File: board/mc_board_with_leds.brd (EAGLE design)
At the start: 73.8 x 40.1 mm, 36 parts, among them IC1 TPS61070DDC, IC2 MEGA8-P, Q2 16MHz

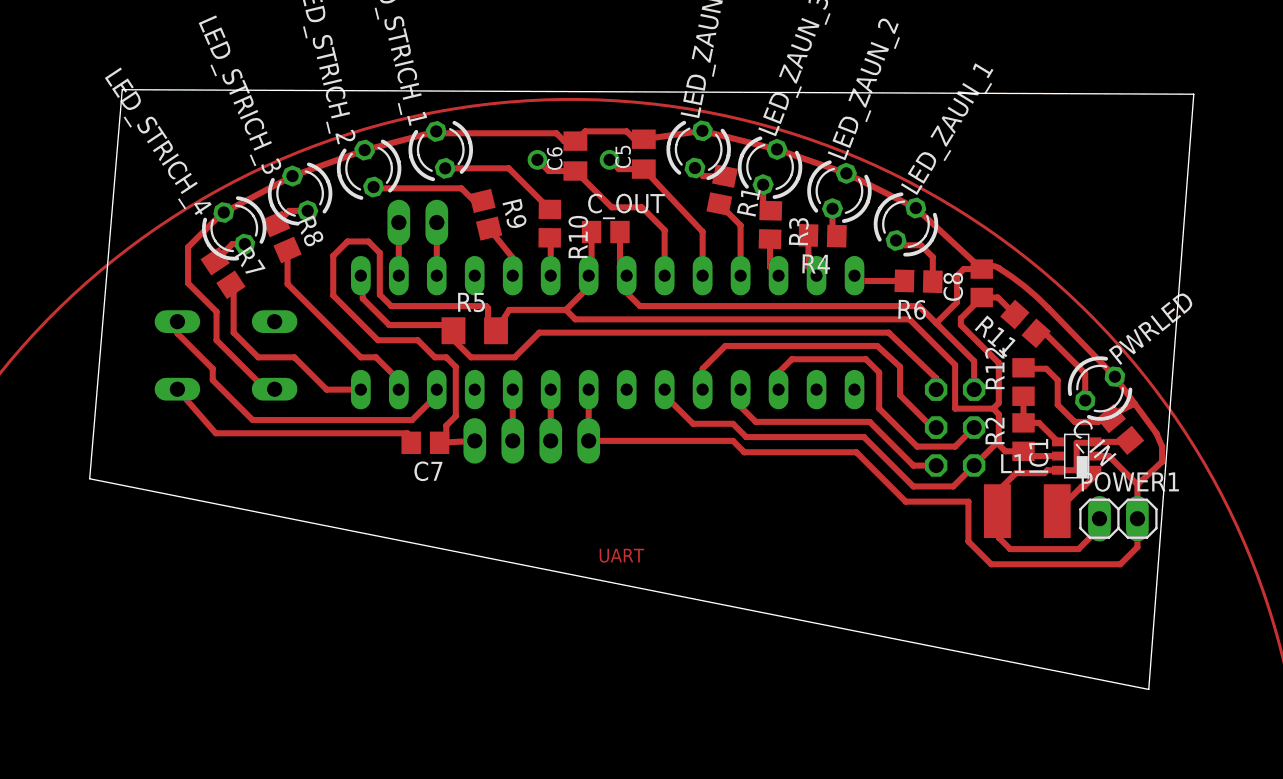
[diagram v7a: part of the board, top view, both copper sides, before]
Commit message: added names to board
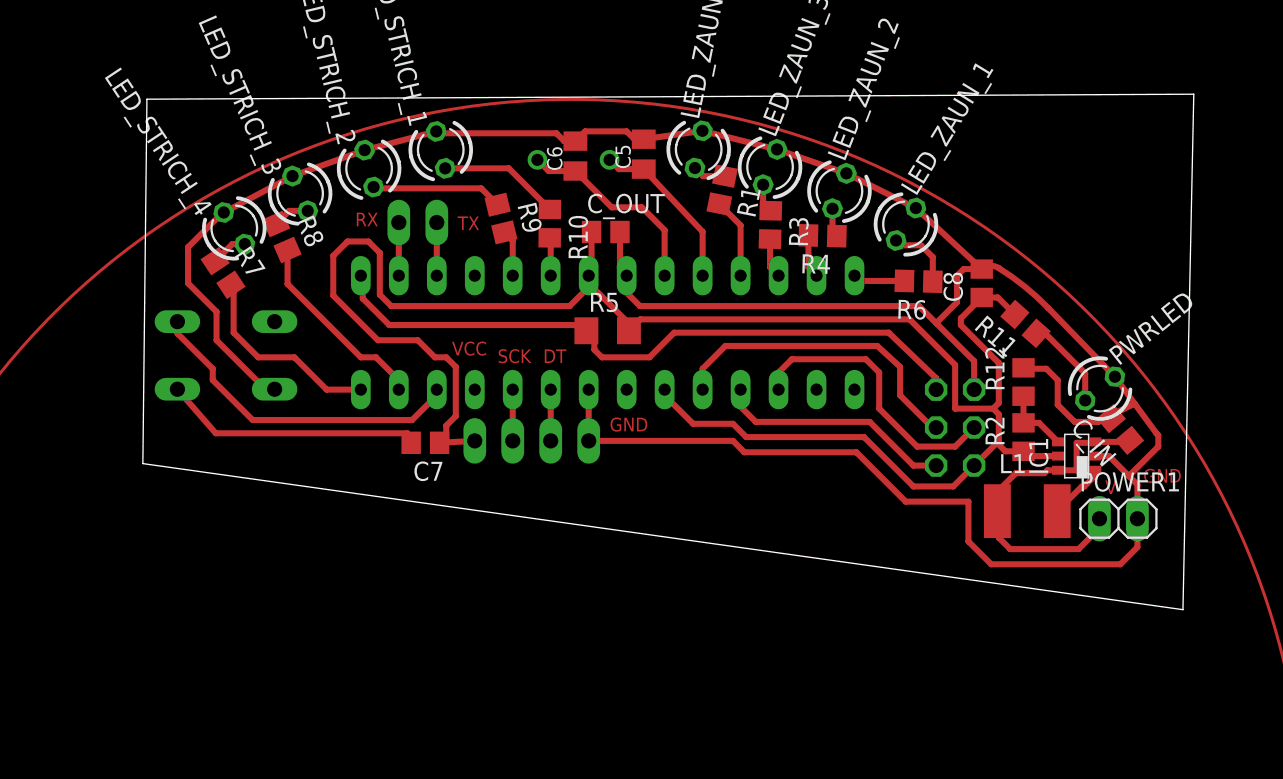
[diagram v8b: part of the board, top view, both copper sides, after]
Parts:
- moved R5 8.89 mm to (51.4, 33.5)
- moved R9 1.05 mm to (44.3, 41.0)
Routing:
- net +5V: track 126.5 -> 124.4 mm
- net N$11: track 7.67 -> 8.79 mm
- net PD3/LED_STRICH_2: track 3.71 -> 3.13 mm
- net GND: track 192.8 -> 192.3 mm
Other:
- board size 73.8 x 40.1 mm -> 70.3 x 34.5 mm
- board text added: "DT"
- board text added: "GND"
- board text added: "RX"
- board text added: "SCK"
- board text added: "TX"
- board text added: "V"
- board text added: "VCC"
- board text removed: "UART"
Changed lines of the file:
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@@
 <board>
 <plain>
-<text x="50.8" y="18.034" size="0.9144" layer="1" font="vector" ratio="28">UART</text>
-<wire x1="16.789471875" y1="23.62764375" x2="18.966596875" y2="49.651115625" width="0" layer="20"/>
-<wire x1="18.966596875" y1="49.651115625" x2="90.63675" y2="49.349575" width="0" layer="20"/>
-<wire x1="90.63675" y1="49.349575" x2="87.626409375" y2="9.53845" width="0" layer="20"/>
-<wire x1="87.626409375" y1="9.53845" x2="16.789471875" y2="23.62764375" width="0" layer="20"/>
+<wire x1="20.345471875" y1="24.64364375" x2="20.617596875" y2="49.016115625" width="0" layer="20"/>
+<wire x1="20.617596875" y1="49.016115625" x2="90.63675" y2="49.349575" width="0" layer="20"/>
+<wire x1="90.63675" y1="49.349575" x2="89.912409375" y2="14.87245" width="0" layer="20"/>
+<wire x1="89.912409375" y1="14.87245" x2="20.345471875" y2="24.64364375" width="0" layer="20"/>
 <circle x="49" y="0" radius="49" width="0.2" layer="1"/>
+<text x="34.544" y="40.513" size="0.9144" layer="1" font="vector" ratio="28">RX</text>
+<text x="41.402" y="40.259" size="0.9144" layer="1" font="vector" ratio="28">TX</text>
+<text x="51.562" y="26.797" size="0.9144" layer="1" font="vector" ratio="28">GND</text>
+<text x="87.249" y="23.368" size="0.9144" layer="1" font="vector" ratio="28">GND</text>
+<text x="84.709" y="22.606" size="0.9144" layer="1" font="vector" ratio="28">V</text>
+<text x="47.117" y="31.369" size="0.9144" layer="1" font="vector" ratio="28">DT</text>
+<text x="44.069" y="31.369" size="0.9144" layer="1" font="vector" ratio="28">SCK</text>
+<text x="41.021" y="31.877" size="0.9144" layer="1" font="vector" ratio="28">VCC</text>
 </plain>
 <attributes>
@@
 <element name="R7" library="resistor" package="R0805" value="470" x="25.7096625" y="37.39071875" rot="R303.6"/>
 <element name="R8" library="resistor" package="R0805" value="470" x="29.6424875" y="39.798434375" rot="R293.6"/>
-<element name="R9" library="resistor" package="R0805" value="470" x="43.281534375" y="41.287296875" rot="R283.6"/>
+<element name="R9" library="resistor" package="R0805" value="470" x="44.297534375" y="41.033296875" rot="R283.6"/>
 <element name="R10" library="resistor" package="R0805" value="470" x="47.565540625" y="40.692409375" rot="R269.6"/>
 <element name="R11" library="resistor" package="R0805" value="470" x="79.383846875" y="33.986165625" rot="R138.6"/>
@@
 <attribute name="OC_FARNELL" value="176432" x="36.703" y="26.162" size="1.778" layer="28" rot="MR0" display="off"/>
 </element>
-<element name="R5" library="rcl-2" package="R1206" value="10k" x="42.545" y="33.528"/>
+<element name="R5" library="rcl-2" package="R1206" value="10k" x="51.435" y="33.528"/>
 <element name="ISP1" library="con-panduit" package="057-006-1" value="ISP-Connector" x="74.676" y="27.051" rot="MR90">
 <attribute name="MPN" value="" x="25.527" y="16.383" size="1.778" layer="28" rot="MR90" display="off"/>
@@
 <wire x1="25.691109375" y1="41.439109375" x2="25.757203125" y2="41.439109375" width="0.4064" layer="1"/>
 <wire x1="84.054" y1="25.146" x2="84.963" y2="25.146" width="0.4064" layer="1"/>
-<wire x1="84.963" y1="25.146" x2="86.868" y2="23.241" width="0.4064" layer="1"/>
+<wire x1="84.963" y1="25.146" x2="86.2965" y2="23.8125" width="0.4064" layer="1"/>
+<wire x1="86.2965" y1="23.8125" x2="86.868" y2="23.241" width="0.4064" layer="1"/>
 <wire x1="86.868" y1="23.241" x2="86.868" y2="20.955" width="0.4064" layer="1"/>
 <wire x1="85.360259375" y1="30.4531125" x2="86.6831" y2="28.651484375" width="0.4064" layer="1"/>
 <wire x1="86.6831" y1="28.651484375" x2="88.138" y2="26.67" width="0.4064" layer="1"/>
-<wire x1="88.138" y1="26.67" x2="88.519" y2="25.781" width="0.4064" layer="1"/>
-<wire x1="88.519" y1="25.781" x2="88.519" y2="24.765" width="0.4064" layer="1"/>
-<wire x1="88.519" y1="24.765" x2="86.868" y2="23.241" width="0.4064" layer="1"/>
 <wire x1="84.201" y1="27.432" x2="85.11435" y2="27.651740625" width="0.4064" layer="1"/>
 <wire x1="84.201" y1="27.432" x2="86.6831" y2="28.651484375" width="0.4064" layer="1"/>
+<wire x1="88.138" y1="26.67" x2="88.265" y2="26.543" width="0.4064" layer="1"/>
+<wire x1="88.265" y1="26.543" x2="88.265" y2="25.781" width="0.4064" layer="1"/>
+<wire x1="88.265" y1="25.781" x2="86.2965" y2="23.8125" width="0.4064" layer="1"/>
 </signal>
 <signal name="+5V">
@@
 <contactref element="HX1" pad="4"/>
 <wire x1="50.165" y1="37.211" x2="50.165" y2="36.449" width="0.4064" layer="1"/>
-<wire x1="50.165" y1="36.449" x2="48.641" y2="34.925" width="0.4064" layer="1"/>
-<wire x1="48.641" y1="34.925" x2="44.856" y2="34.925" width="0.4064" layer="1"/>
-<wire x1="44.856" y1="34.925" x2="43.967" y2="33.528" width="0.4064" layer="1"/>
-<wire x1="48.641" y1="34.925" x2="49.276" y2="34.29" width="0.4064" layer="1"/>
-<wire x1="49.276" y1="34.29" x2="71.628" y2="34.29" width="0.4064" layer="1"/>
 <wire x1="71.628" y1="34.29" x2="74.676" y2="31.242" width="0.4064" layer="1"/>
 <wire x1="74.676" y1="31.242" x2="74.676" y2="28.321" width="0.4064" layer="1"/>
@@
 <wire x1="77.597" y1="26.162" x2="77.47" y2="26.035" width="0.4064" layer="1"/>
 <wire x1="77.47" y1="26.035" x2="75.946" y2="24.511" width="0.4064" layer="1"/>
-<wire x1="43.967" y1="33.528" x2="43.434" y2="34.061" width="0.4064" layer="1"/>
-<wire x1="43.434" y1="34.061" x2="43.434" y2="35.052" width="0.4064" layer="1"/>
-<wire x1="43.434" y1="35.052" x2="43.307" y2="35.179" width="0.4064" layer="1"/>
-<wire x1="43.307" y1="35.179" x2="36.957" y2="35.179" width="0.4064" layer="1"/>
 <wire x1="36.957" y1="35.179" x2="36.195" y2="35.941" width="0.4064" layer="1"/>
 <wire x1="36.195" y1="35.941" x2="36.195" y2="38.735" width="0.4064" layer="1"/>
@@
 <wire x1="79.248" y1="25.466" x2="78.039" y2="25.466" width="0.4064" layer="1"/>
 <wire x1="78.039" y1="25.466" x2="77.47" y2="26.035" width="0.4064" layer="1"/>
+<wire x1="71.628" y1="34.29" x2="53.619" y2="34.29" width="0.4064" layer="1"/>
+<wire x1="50.165" y1="36.449" x2="48.895" y2="35.179" width="0.4064" layer="1"/>
+<wire x1="48.895" y1="35.179" x2="36.957" y2="35.179" width="0.4064" layer="1"/>
+<wire x1="53.619" y1="34.29" x2="52.857" y2="33.528" width="0.4064" layer="1"/>
+<wire x1="50.165" y1="36.449" x2="50.419" y2="36.449" width="0.4064" layer="1"/>
+<wire x1="50.419" y1="36.449" x2="52.578" y2="34.29" width="0.4064" layer="1"/>
+<wire x1="52.578" y1="34.29" x2="52.578" y2="33.807" width="0.4064" layer="1"/>
+<wire x1="52.578" y1="33.807" x2="52.857" y2="33.528" width="0.4064" layer="1"/>
 </signal>
 <signal name="PB4/MISO">
@@
 <contactref element="IC2" pad="5"/>
 <contactref element="R9" pad="2"/>
-<wire x1="45.085" y1="37.211" x2="45.085" y2="38.40285" width="0.4064" layer="1"/>
-<wire x1="45.085" y1="38.40285" x2="43.50491875" y2="40.36393125" width="0.4064" layer="1"/>
+<wire x1="45.085" y1="37.211" x2="45.085" y2="37.719" width="0.4064" layer="1"/>
+<wire x1="45.085" y1="37.719" x2="45.085" y2="38.40285" width="0.4064" layer="1"/>
+<wire x1="44.52091875" y1="40.10993125" x2="45.085" y2="39.54585" width="0.4064" layer="1"/>
+<wire x1="45.085" y1="39.54585" x2="45.085" y2="38.40285" width="0.4064" layer="1"/>
 </signal>
 <signal name="PD4/LED_STRICH_1">
@@
 <wire x1="73.406" y1="29.591" x2="73.406" y2="30.353" width="0.4064" layer="1"/>
 <wire x1="73.406" y1="30.353" x2="70.231" y2="33.401" width="0.4064" layer="1"/>
-<wire x1="70.231" y1="33.401" x2="46.863" y2="33.401" width="0.4064" layer="1"/>
-<wire x1="46.863" y1="33.401" x2="45.212" y2="31.75" width="0.4064" layer="1"/>
-<wire x1="40.996" y1="33.045" x2="41.123" y2="33.528" width="0.4064" layer="1"/>
-<wire x1="45.212" y1="31.75" x2="42.291" y2="31.75" width="0.4064" layer="1"/>
-<wire x1="42.291" y1="31.75" x2="40.996" y2="33.045" width="0.4064" layer="1"/>
-<wire x1="36.83" y1="33.909" x2="40.742" y2="33.909" width="0.4064" layer="1"/>
-<wire x1="40.742" y1="33.909" x2="41.123" y2="33.528" width="0.4064" layer="1"/>
+<wire x1="36.83" y1="33.909" x2="49.632" y2="33.909" width="0.4064" layer="1"/>
+<wire x1="49.632" y1="33.909" x2="50.013" y2="33.528" width="0.4064" layer="1"/>
+<wire x1="70.231" y1="33.401" x2="55.88" y2="33.401" width="0.4064" layer="1"/>
+<wire x1="55.88" y1="33.401" x2="54.229" y2="31.75" width="0.4064" layer="1"/>
+<wire x1="54.229" y1="31.75" x2="51.054" y2="31.75" width="0.4064" layer="1"/>
+<wire x1="51.054" y1="31.75" x2="50.546" y2="32.258" width="0.4064" layer="1"/>
+<wire x1="50.546" y1="32.258" x2="50.546" y2="32.995" width="0.4064" layer="1"/>
+<wire x1="50.546" y1="32.995" x2="50.013" y2="33.528" width="0.4064" layer="1"/>
 </signal>
 <signal name="VDD">
@@
 <contactref element="LED_STRICH_2" pad="A"/>
 <wire x1="35.775934375" y1="43.140675" x2="35.863609375" y2="43.053" width="0.4064" layer="1"/>
-<wire x1="35.863609375" y1="43.053" x2="41.656" y2="43.053" width="0.4064" layer="1"/>
-<wire x1="41.656" y1="43.053" x2="42.498340625" y2="42.210659375" width="0.4064" layer="1"/>
-<wire x1="42.498340625" y1="42.210659375" x2="43.058146875" y2="42.210659375" width="0.4064" layer="1"/>
+<wire x1="35.863609375" y1="43.053" x2="42.97780625" y2="43.053" width="0.4064" layer="1"/>
+<wire x1="44.074146875" y1="41.956659375" x2="42.97780625" y2="43.053" width="0.4064" layer="1"/>
 </signal>
 <signal name="N$12">
@@
 </signal>
 </signals>
+<errors>
+</errors>
 </board>
 </drawing>
